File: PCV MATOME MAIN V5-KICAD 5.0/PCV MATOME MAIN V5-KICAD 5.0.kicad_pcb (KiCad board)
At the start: 2 copper layers, 101.6 x 53.3 mm, 14 parts, among them P1 Digital, P10 CONN_01X01, P11 CONN_01X01, P12 CONN_01X01, P13 CONN_01X01, P2 Power, P3 Analog, P4 Analog, P5 PWM, P6 PWM, P7 Communication, P8 CONN_01X01, P9 CONN_01X01, U1 ESP-12F

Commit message: initinal pcb
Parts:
- added C1: 100n, Capacitor_SMD:C_0805_2012Metric_Pad1.15x1.40mm_HandSolder, F.Cu at (113.5, 23.7)
- added C10: 100n, Capacitor_SMD:C_0805_2012Metric_Pad1.15x1.40mm_HandSolder, F.Cu at (52.2, 71.7)
- added C11: 100n, Capacitor_SMD:C_0805_2012Metric_Pad1.15x1.40mm_HandSolder, F.Cu at (111.7, 37.1)
- added C12: 100n, Capacitor_SMD:C_0805_2012Metric_Pad1.15x1.40mm_HandSolder, F.Cu at (102.4, 50.4)
- added C13: 100n, Capacitor_SMD:C_0805_2012Metric_Pad1.15x1.40mm_HandSolder, F.Cu at (106.2, 48.4)
- added C14: 100n, Capacitor_SMD:C_0805_2012Metric_Pad1.15x1.40mm_HandSolder, F.Cu at (102.4, 48.4)
- added C15: 100n, Capacitor_SMD:C_0805_2012Metric_Pad1.15x1.40mm_HandSolder, F.Cu at (106.2, 46.5)
- added C16: 100n, Capacitor_SMD:C_0805_2012Metric_Pad1.15x1.40mm_HandSolder, F.Cu at (80.5, 71.3)
- added C17: 100n, Capacitor_SMD:C_0805_2012Metric_Pad1.15x1.40mm_HandSolder, F.Cu at (84.2, 67.4)
- added C18: 100n, Capacitor_SMD:C_0805_2012Metric_Pad1.15x1.40mm_HandSolder, F.Cu at (115.4, 37.3)
- added C19: 100n, Capacitor_SMD:C_0805_2012Metric_Pad1.15x1.40mm_HandSolder, F.Cu at (111.7, 41.0)
- added C2: 100n, Capacitor_SMD:C_0805_2012Metric_Pad1.15x1.40mm_HandSolder, F.Cu at (113.5, 21.7)
- added C20: 100n, Capacitor_SMD:C_0805_2012Metric_Pad1.15x1.40mm_HandSolder, F.Cu at (59.6, 39.2)
- added C21: 100n, Capacitor_SMD:C_0805_2012Metric_Pad1.15x1.40mm_HandSolder, F.Cu at (91.5, 42.4)
- added C22: 100n, Capacitor_SMD:C_0805_2012Metric_Pad1.15x1.40mm_HandSolder, F.Cu at (91.5, 40.5)
- added C23: 100n, Capacitor_SMD:C_0805_2012Metric_Pad1.15x1.40mm_HandSolder, F.Cu at (91.5, 38.5)
- added C24: 100n, Capacitor_SMD:C_0805_2012Metric_Pad1.15x1.40mm_HandSolder, F.Cu at (113.5, 27.6)
- added C25: 10u, Capacitor_SMD:C_0805_2012Metric_Pad1.15x1.40mm_HandSolder, F.Cu at (113.5, 25.6)
- added C26: 10u, Capacitor_SMD:CP_Elec_4x5.4, F.Cu at (58.1, 43.3)
- added C27: 100u, Capacitor_SMD:CP_Elec_8x6.5, F.Cu at (75.7, 49.5)
- added C28: 100u, Capacitor_SMD:CP_Elec_8x6.5, F.Cu at (95.2, 48.0)
- added C3: 100n, Capacitor_SMD:C_0805_2012Metric_Pad1.15x1.40mm_HandSolder, F.Cu at (113.5, 19.8)
- added C4: 100n, Capacitor_SMD:C_0805_2012Metric_Pad1.15x1.40mm_HandSolder, F.Cu at (59.6, 37.2)
- added C5: 100n, Capacitor_SMD:C_0805_2012Metric_Pad1.15x1.40mm_HandSolder, F.Cu at (39.7, 63.5)
- added C6: 100n, Capacitor_SMD:C_0805_2012Metric_Pad1.15x1.40mm_HandSolder, F.Cu at (37.2, 71.7)
- added C7: 100n, Capacitor_SMD:C_0805_2012Metric_Pad1.15x1.40mm_HandSolder, F.Cu at (41.0, 71.7)
- added C8: 100n, Capacitor_SMD:C_0805_2012Metric_Pad1.15x1.40mm_HandSolder, F.Cu at (44.7, 71.7)
- added C9: 100n, Capacitor_SMD:C_0805_2012Metric_Pad1.15x1.40mm_HandSolder, F.Cu at (48.5, 71.7)
- added D1: D, Diode_SMD:D_SOD-123, F.Cu at (60.1, 35.1)
- added D2: D, Diode_SMD:D_SOD-123, F.Cu at (60.1, 32.7)
- added D3: D, Diode_SMD:D_SOD-123, F.Cu at (60.3, 29.4)
- added D4: D, Diode_SMD:D_SOD-123, F.Cu at (40.2, 61.3)
- added J1: Conn_02x08_Odd_Even, Connector_IDC:IDC-Header_2x08_P2.54mm_Vertical, F.Cu at (262.9, 62.2)
- added J10: Conn_01x02, Connector_JST:JST_EH_B02B-EH-A_1x02_P2.50mm_Vertical, F.Cu at (92.7, 59.6)
- added J11: Conn_01x04, Connector_JST:JST_EH_B04B-EH-A_1x04_P2.50mm_Vertical, F.Cu at (121.4, 59.9)
- added J12: Conn_01x08, Connector_JST:JST_EH_B08B-EH-A_1x08_P2.50mm_Vertical, F.Cu at (86.9, 141.5)
- added J13: Conn_01x08, Connector_JST:JST_EH_B08B-EH-A_1x08_P2.50mm_Vertical, F.Cu at (43.9, 143.0)
- added J14: Conn_01x02, Connector_Wire:SolderWirePad_1x02_P5.08mm_Drill1.5mm, F.Cu at (49.8, 57.7)
- added J15: Conn_01x02, Connector_Wire:SolderWirePad_1x02_P5.08mm_Drill1.5mm, F.Cu at (63.2, 61.0)
- added J2: Conn_02x08_Odd_Even, Connector_IDC:IDC-Header_2x08_P2.54mm_Vertical, F.Cu at (225.3, 62.5)
- added J3: Conn_01x06, Connector_JST:JST_EH_B06B-EH-A_1x06_P2.50mm_Vertical, F.Cu at (236.2, 102.9)
- added J4: Conn_01x06, Connector_JST:JST_EH_B06B-EH-A_1x06_P2.50mm_Vertical, F.Cu at (264.2, 93.7)
- added J6: Conn_01x06, Connector_JST:JST_EH_B06B-EH-A_1x06_P2.50mm_Vertical, F.Cu at (236.2, 94.0)
- added J7: Conn_01x06, Connector_JST:JST_EH_B06B-EH-A_1x06_P2.50mm_Vertical, F.Cu at (264.2, 102.9)
- added J8: Conn_01x08, Connector_JST:JST_EH_B08B-EH-A_1x08_P2.50mm_Vertical, F.Cu at (28.2, 111.0)
- added J9: Conn_01x16, Connector_JST:JST_EH_B16B-EH-A_1x16_P2.50mm_Vertical, F.Cu at (142.2, 132.1)
- added Q1: BSS138, Package_TO_SOT_SMD:SOT-23, F.Cu at (84.1, 70.2)
- added Q2: BSS138, Package_TO_SOT_SMD:SOT-23, F.Cu at (87.8, 67.5)
- added Q3: 2SC1815, Package_TO_SOT_THT:TO-92_Inline, F.Cu at (31.3, 72.3)
- added R1: 10K, Resistor_SMD:R_0805_2012Metric_Pad1.15x1.40mm_HandSolder, F.Cu at (102.4, 46.5)
- added R10: 10K, Resistor_SMD:R_0805_2012Metric_Pad1.15x1.40mm_HandSolder, F.Cu at (88.0, 64.7)
- added R11: 10K, Resistor_SMD:R_0805_2012Metric_Pad1.15x1.40mm_HandSolder, F.Cu at (111.7, 39.1)
- added R12: 10K, Resistor_SMD:R_0805_2012Metric_Pad1.15x1.40mm_HandSolder, F.Cu at (115.4, 35.4)
- added R13: 10K, Resistor_SMD:R_0805_2012Metric_Pad1.15x1.40mm_HandSolder, F.Cu at (100.1, 53.4)
- added R14: 10K, Resistor_SMD:R_0805_2012Metric_Pad1.15x1.40mm_HandSolder, F.Cu at (111.7, 35.2)
- added R15: 10K, Resistor_SMD:R_0805_2012Metric_Pad1.15x1.40mm_HandSolder, F.Cu at (84.2, 65.5)
- added R16: 10K, Resistor_SMD:R_0805_2012Metric_Pad1.15x1.40mm_HandSolder, F.Cu at (80.5, 69.4)
- added R17: 10K, Resistor_SMD:R_0805_2012Metric_Pad1.15x1.40mm_HandSolder, F.Cu at (115.4, 33.4)
- added R18: 100, Resistor_SMD:R_0805_2012Metric_Pad1.15x1.40mm_HandSolder, F.Cu at (80.5, 67.4)
- added R2: 10K, Resistor_SMD:R_0805_2012Metric_Pad1.15x1.40mm_HandSolder, F.Cu at (106.2, 44.5)
- added R3: 20K, Resistor_SMD:R_0805_2012Metric_Pad1.15x1.40mm_HandSolder, F.Cu at (91.4, 62.8)
- added R4: 10K, Resistor_SMD:R_0805_2012Metric_Pad1.15x1.40mm_HandSolder, F.Cu at (102.4, 44.5)
- added R5: 10K, Resistor_SMD:R_0805_2012Metric_Pad1.15x1.40mm_HandSolder, F.Cu at (80.5, 65.5)
- added R6: 10K, Resistor_SMD:R_0805_2012Metric_Pad1.15x1.40mm_HandSolder, F.Cu at (80.5, 63.5)
- added R7: 10K, Resistor_SMD:R_0805_2012Metric_Pad1.15x1.40mm_HandSolder, F.Cu at (113.5, 31.5)
- added R8: 10K, Resistor_SMD:R_0805_2012Metric_Pad1.15x1.40mm_HandSolder, F.Cu at (113.5, 29.5)
- added R9: 10K, Resistor_SMD:R_0805_2012Metric_Pad1.15x1.40mm_HandSolder, F.Cu at (84.2, 63.5)
- added RN1: R_Network08, Resistor_THT:R_Array_SIP9, F.Cu at (31.8, 21.8)
- added RN2: R_Network08, Resistor_THT:R_Array_SIP9, F.Cu at (15.2, 53.3)
- added RV1: R_POT, Potentiometer_THT:Potentiometer_Bourns_3296W_Vertical, F.Cu at (46.2, 34.3)
- added SW1: SW_Push, Button_Switch_THT:SW_DIP_SPSTx01_Slide_9.78x4.72mm_W7.62mm_P2.54mm, F.Cu at (35.6, 43.6)
- added U2: MAX7219, Package_SO:SOIC-24W_7.5x15.4mm_P1.27mm, F.Cu at (273.1, 78.7)
- added U3: MAX7219, Package_SO:SOIC-24W_7.5x15.4mm_P1.27mm, F.Cu at (233.7, 78.7)
- added U4: LM1117-3.3, Package_TO_SOT_SMD:SOT-223-3_TabPin2, F.Cu at (69.3, 77.5)
- added U5: LD1117S50TR_SOT223, Package_TO_SOT_THT:TO-220-3_Vertical, F.Cu at (17.3, 81.8)
- added U6: SHIFT_LEVEL_3.3V_5V, LEEVAWNS:SHIFTLEVEL, F.Cu at (197.6, 131.1)
- moved U1 30.9 mm to (236.2, 137.2)
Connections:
- net +5V renamed HV
- P1 pad 10: (no net) -> RESET_ESP
- P1 pad 11: (no net) -> SW14
- P1 pad 12: (no net) -> SW15
- P1 pad 13: (no net) -> SW12
- P1 pad 14: (no net) -> SW13
- P1 pad 15: (no net) -> SW10
- P1 pad 16: (no net) -> SW11
- P1 pad 17: (no net) -> SW8
- P1 pad 18: (no net) -> SW9
- P1 pad 19: (no net) -> SW6
- P1 pad 20: (no net) -> SW7
- P1 pad 21: (no net) -> SW4
- P1 pad 22: (no net) -> SW5
- P1 pad 23: (no net) -> SW2
- P1 pad 24: (no net) -> SW3
- P1 pad 25: (no net) -> SC4
- P1 pad 26: (no net) -> SW1
- P1 pad 27: (no net) -> SC2
- P1 pad 28: (no net) -> SC3
- P1 pad 29: (no net) -> SCK
- P1 pad 30: (no net) -> SC1
- P1 pad 31: (no net) -> CLK_M
- P1 pad 32: (no net) -> DIN
- P1 pad 33: (no net) -> DIN_M
- P1 pad 34: (no net) -> SC_M
- P1 pad 9: (no net) -> SW16
- P2 pad 4: (no net) -> LV
- P2 pad 8: (no net) -> /Vin
- P3 pad 1: (no net) -> RS
- P3 pad 2: (no net) -> RW
- P3 pad 3: (no net) -> EN
- P3 pad 4: (no net) -> D4
- P3 pad 5: (no net) -> D5
- P3 pad 6: (no net) -> D6
- P3 pad 7: (no net) -> D7
- P5 pad 1: (no net) -> SCL
- P5 pad 2: (no net) -> SDA
- P6 pad 2: (no net) -> SET
- P6 pad 3: (no net) -> HOME
- P6 pad 4: (no net) -> BACK
- P6 pad 5: (no net) -> NEXT
- P6 pad 6: (no net) -> BUZZER
- P7 pad 5: (no net) -> RX5V
- P7 pad 6: (no net) -> TX5V
- U1 pad 1: (no net) -> Net-(R1-Pad2)
- U1 pad 15: (no net) -> GND
- U1 pad 16: (no net) -> Net-(R5-Pad2)
- U1 pad 17: (no net) -> Net-(R7-Pad2)
- U1 pad 18: (no net) -> Net-(R6-Pad2)
- U1 pad 21: (no net) -> RX3.3V
- U1 pad 22: (no net) -> TX3.3V
- U1 pad 3: (no net) -> Net-(R2-Pad1)
- U1 pad 8: (no net) -> LV

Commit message: initilize pcb layout
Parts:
- P1: renamed from P2; moved to B.Cu
- P10, P11, P12, P13, P5, P6, P7, P8, P9: moved to B.Cu
- P2: renamed from P3; moved to B.Cu
- P3: renamed from P4; moved to B.Cu
- P4: renamed from P1; moved to B.Cu
- moved SW1 221.1 mm to (240.6, 126.5), turned to 180 degrees
- moved RN2 200.4 mm to (215.6, 57.1), turned to 180 degrees
- moved C4 183.1 mm to (236.2, 85.3)
- moved J12 177.9 mm to (195.6, 50.0)
- moved C1 164.9 mm to (238.3, 131.6), turned to 180 degrees
- moved R1 161.7 mm to (233.4, 141.3), turned to 90 degrees
- moved R3 160.3 mm to (233.4, 136.9), turned to 90 degrees
- moved RN1 159.4 mm to (187.5, 55.9), turned to 180 degrees
- moved R2 154.4 mm to (233.2, 132.3), turned to 90 degrees
- moved C2 153.9 mm to (231.6, 120.4), turned to 90 degrees
- moved C20 153.7 mm to (211.1, 65.0)
- moved J7 152.0 mm to (167.1, 49.3)
- moved Q3 146.8 mm to (167.9, 126.2), turned to 180 degrees
- moved R4 145.9 mm to (235.7, 103.9)
- moved R6 145.2 mm to (208.5, 132.1)
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- renumbered J11 to J10, J12 to J11, J13 to J12, J14 to J13, J15 to J14, J6 to J5, J7 to J6, J8 to J7, J9 to J8, J10 to J9, U2 to U1, U1 to U2, U6 to U4, U4 to U5, U5 to U6
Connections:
- J3 pad 6: (no net) -> Net-(J3-Pad6)
- J4 pad 6: (no net) -> Net-(J4-Pad6)
- J5 pad 6: (no net) -> Net-(J5-Pad6)
- J6 pad 6: (no net) -> Net-(J6-Pad6)
- J8 pad 10: (no net) -> Net-(J8-Pad10)
- J8 pad 7: (no net) -> Net-(J8-Pad7)
- J8 pad 8: (no net) -> Net-(J8-Pad8)
- J8 pad 9: (no net) -> Net-(J8-Pad9)
- P1 pad 1: (no net) -> Net-(P1-Pad1)
- P1 pad 2: (no net) -> /IOREF
- P1 pad 3: (no net) -> /Reset
- P10 pad 1: (no net) -> Net-(P10-Pad1)
- P11 pad 1: (no net) -> Net-(P11-Pad1)
- P12 pad 1: (no net) -> Net-(P12-Pad1)
- P13 pad 1: (no net) -> Net-(P13-Pad1)
- P2 pad 8: (no net) -> /A7
- P3 pad 1: (no net) -> /A8
- P3 pad 2: (no net) -> /A9
- P3 pad 3: (no net) -> /A10
- P3 pad 4: (no net) -> /A11
- P3 pad 5: (no net) -> /A12
- P3 pad 6: (no net) -> /A13
- P3 pad 7: (no net) -> /A14
- P3 pad 8: (no net) -> /A15
- P4 pad 3: (no net) -> /52(SCK)
- P4 pad 4: (no net) -> /53(SS)
- P4 pad 5: (no net) -> /50(MISO)
- P4 pad 6: (no net) -> /51(MOSI)
- P4 pad 7: (no net) -> /48
- P4 pad 8: (no net) -> /49
- P5 pad 10: (no net) -> /8(**)
- P5 pad 3: (no net) -> /AREF
- P5 pad 5: (no net) -> /13(**)
- P5 pad 6: (no net) -> /12(**)
- P5 pad 7: (no net) -> /11(**)
- P5 pad 8: (no net) -> /10(**)
- P5 pad 9: (no net) -> /9(**)
- P6 pad 1: (no net) -> /7(**)
- P6 pad 7: (no net) -> /1(Tx0)
- P6 pad 8: (no net) -> /0(Rx0)
- P7 pad 1: (no net) -> /14(Tx3)
- P7 pad 2: (no net) -> /15(Rx3)
- P7 pad 3: (no net) -> /16(Tx2)
- P7 pad 4: (no net) -> /17(Rx2)
- P7 pad 7: (no net) -> /20(SDA)
- P7 pad 8: (no net) -> /21(SCL)
- P8 pad 1: (no net) -> Net-(P8-Pad1)
- P9 pad 1: (no net) -> Net-(P9-Pad1)
- U2 pad 10: (no net) -> Net-(U2-Pad10)
- U2 pad 11: (no net) -> Net-(U2-Pad11)
- U2 pad 12: (no net) -> Net-(U2-Pad12)
- U2 pad 13: (no net) -> Net-(U2-Pad13)
- U2 pad 14: (no net) -> Net-(U2-Pad14)
- U2 pad 19: (no net) -> Net-(U2-Pad19)
- U2 pad 2: (no net) -> Net-(U2-Pad2)
- U2 pad 20: (no net) -> Net-(U2-Pad20)
- U2 pad 4: (no net) -> Net-(U2-Pad4)
- U2 pad 5: (no net) -> Net-(U2-Pad5)
- U2 pad 6: (no net) -> Net-(U2-Pad6)
- U2 pad 7: (no net) -> Net-(U2-Pad7)
- U2 pad 9: (no net) -> Net-(U2-Pad9)
- U3 pad 24: (no net) -> Net-(U3-Pad24)
- U4 pad 10: (no net) -> Net-(U4-Pad10)
- U4 pad 3: (no net) -> Net-(U4-Pad3)
- U4 pad 4: (no net) -> Net-(U4-Pad4)
- U4 pad 9: (no net) -> Net-(U4-Pad9)
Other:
- board outline removed

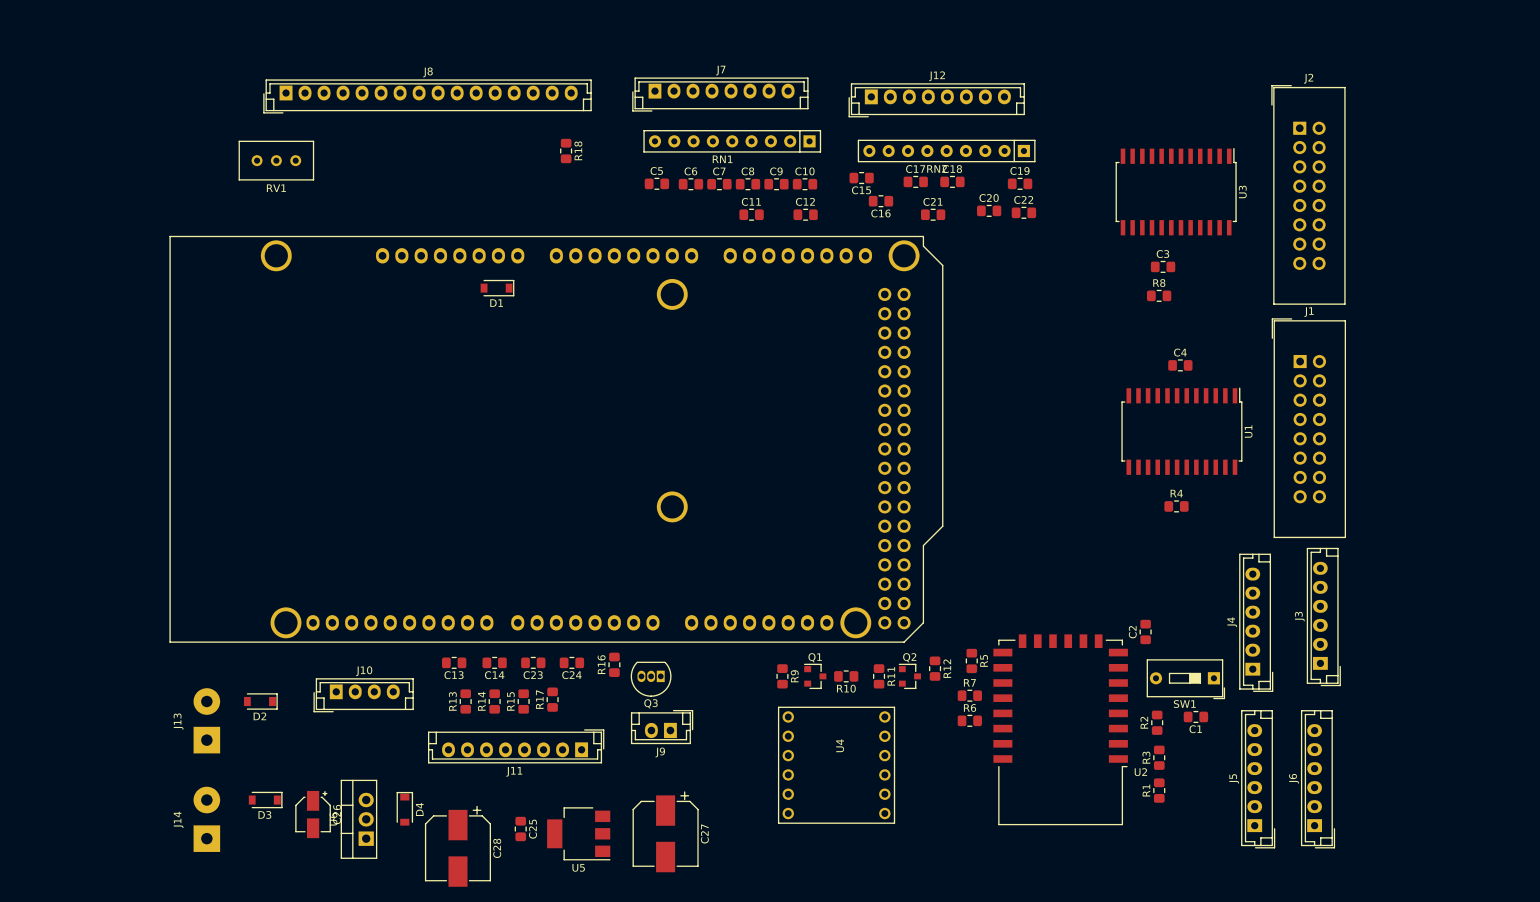
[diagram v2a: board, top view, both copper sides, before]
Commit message: modifier pcb and schematic net list
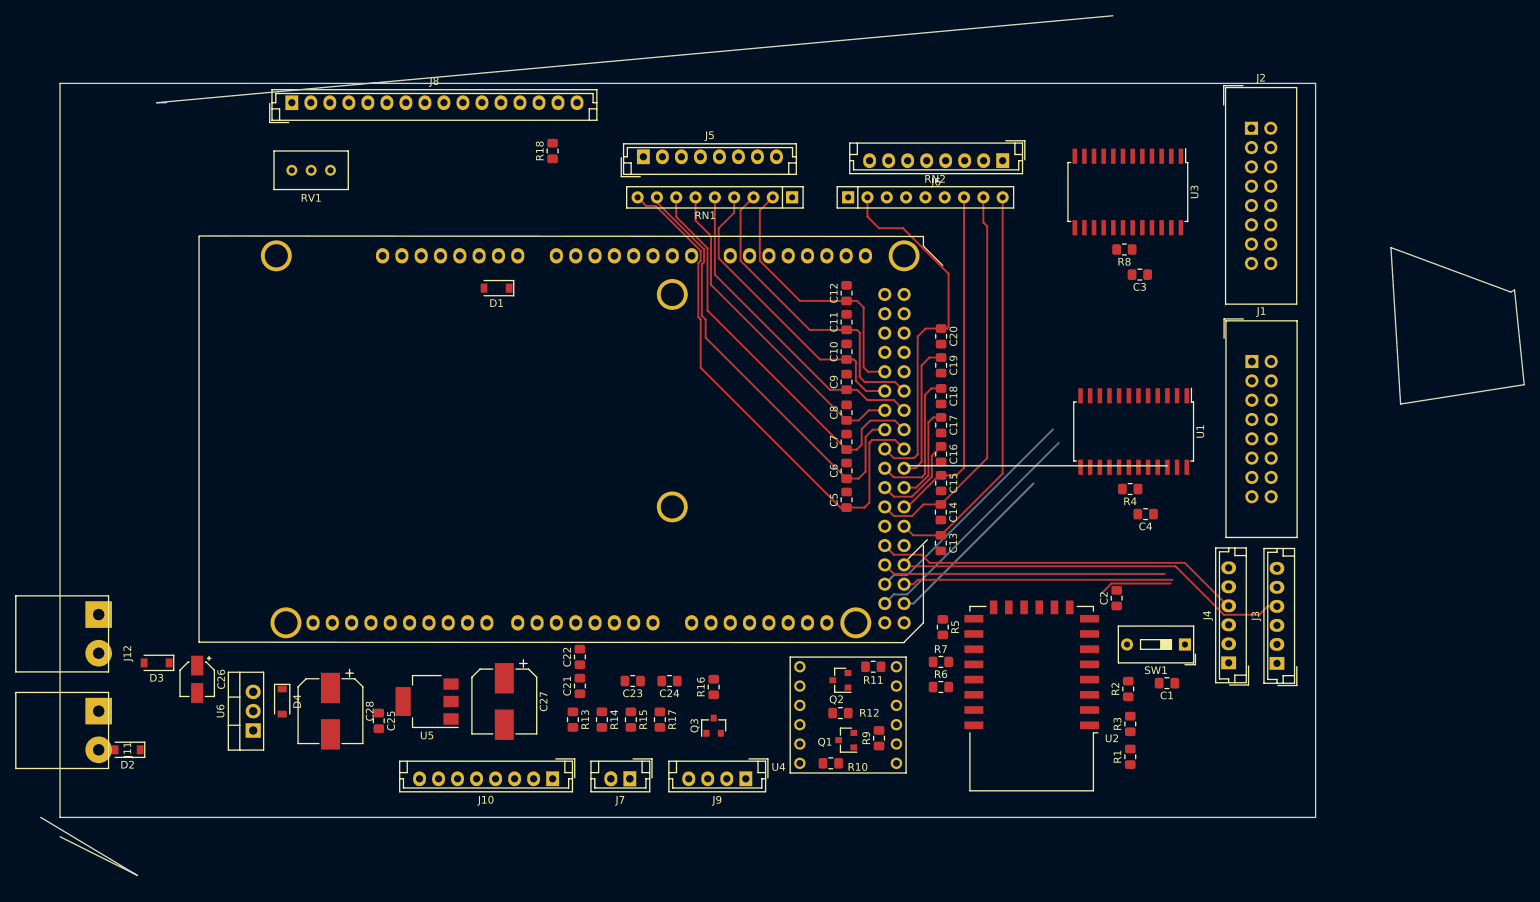
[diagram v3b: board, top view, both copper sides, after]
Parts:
- removed J13, J14: Conn_01x02, Connector_Wire:SolderWirePad_1x02_P5.08mm_Drill1.5mm
- J10: value Conn_01x04 -> Conn_01x08; footprint Connector_JST:JST_EH_B04B-EH-A_1x04_P2.50mm_Vertical -> Connector_JST:JST_EH_B08B-EH-A_1x08_P2.50mm_Vertical
- J11, J12: value Conn_01x08 -> Conn_01x02; footprint Connector_JST:JST_EH_B08B-EH-A_1x08_P2.50mm_Vertical -> LEEVAWNS:SolderWirePad_1x02_P5.08mm_Drill1.5mm
- J5, J6: value Conn_01x06 -> Conn_01x08; footprint Connector_JST:JST_EH_B06B-EH-A_1x06_P2.50mm_Vertical -> Connector_JST:JST_EH_B08B-EH-A_1x08_P2.50mm_Vertical
- J7: value Conn_01x08 -> Conn_01x02; footprint Connector_JST:JST_EH_B08B-EH-A_1x08_P2.50mm_Vertical -> Connector_JST:JST_EH_B02B-EH-A_1x02_P2.50mm_Vertical
- J9: value Conn_01x02 -> Conn_01x04; footprint Connector_JST:JST_EH_B02B-EH-A_1x02_P2.50mm_Vertical -> Connector_JST:JST_EH_B04B-EH-A_1x04_P2.50mm_Vertical
- Q3: footprint Package_TO_SOT_THT:TO-92_Inline -> Package_TO_SOT_SMD:SOT-23
- moved J12 123.7 mm to (94.0, 120.7), turned to 270 degrees
- moved J5 119.2 mm to (165.6, 57.9), turned to 0 degrees
- moved J6 96.6 mm to (212.9, 58.4), turned to 180 degrees
- moved J7 90.5 mm to (163.8, 139.7), turned to 180 degrees
- moved C22 82.6 mm to (157.3, 123.7), turned to 90 degrees
- moved C21 77.4 mm to (157.3, 127.5), turned to 90 degrees
- moved C13 65.9 mm to (204.7, 108.7), turned to 270 degrees
- moved J11 63.6 mm to (94.0, 133.3), turned to 270 degrees
- moved C14 61.9 mm to (204.7, 104.6), turned to 270 degrees
- moved C5 48.5 mm to (192.3, 103.0), turned to 90 degrees
- moved C6 42.9 mm to (192.3, 99.2), turned to 90 degrees
- moved C15 41.5 mm to (204.8, 100.8), turned to 270 degrees
- moved C7 37.8 mm to (192.3, 95.4), turned to 90 degrees
- moved C16 34.2 mm to (204.8, 97.0), turned to 270 degrees
- moved C8 32.7 mm to (192.3, 91.6), turned to 90 degrees
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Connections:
- C13 pad 1: SET -> SW1
- C14 pad 1: HOME -> SW2
- C15 pad 1: SW1 -> SW3
- C16 pad 1: SW2 -> SW4
- C17 pad 1: SW3 -> SW5
- C18 pad 1: SW4 -> SW6
- C19 pad 1: SW5 -> SW7
- C20 pad 1: SW6 -> SW8
- C21 pad 1: SW7 -> SET
- C22 pad 1: SW8 -> HOME
- J10 pad 1: SCL -> NEXT
- J10 pad 2: SDA -> GND
- J10 pad 3: HV -> BACK
- J11 pad 1: NEXT -> GND
- J11 pad 2: GND -> Net-(D2-Pad2)
- J12 pad 1: SW1 -> GND
- J12 pad 2: SW2 -> Net-(D3-Pad2)
- J3 pad 6: Net-(J3-Pad6) -> (no net)
- J4 pad 6: Net-(J4-Pad6) -> (no net)
- J5 pad 1: HV -> SW9
- J5 pad 2: GND -> SW10
- J5 pad 3: DIN -> SW11
- J5 pad 4: SC3 -> SW12
- J5 pad 5: SCK -> SW13
- J5 pad 6: Net-(J5-Pad6) -> SW14
- J6 pad 1: HV -> SW1
- J6 pad 2: GND -> SW2
- J6 pad 3: DIN -> SW3
- J6 pad 4: SC4 -> SW4
- J6 pad 5: SCK -> SW5
- J6 pad 6: Net-(J6-Pad6) -> SW6
- J7 pad 1: SW9 -> HV
- J7 pad 2: SW10 -> Net-(J7-Pad2)
- J8 pad 10: Net-(J8-Pad10) -> (no net)
- J8 pad 7: Net-(J8-Pad7) -> (no net)
- J8 pad 8: Net-(J8-Pad8) -> (no net)
- J8 pad 9: Net-(J8-Pad9) -> (no net)
- J9 pad 1: HV -> SCL
- J9 pad 2: Net-(J9-Pad2) -> SDA
- P1 pad 1: Net-(P1-Pad1) -> (no net)
- P1 pad 2: /IOREF -> (no net)
- P1 pad 3: /Reset -> (no net)
- P10 pad 1: Net-(P10-Pad1) -> (no net)
- P11 pad 1: Net-(P11-Pad1) -> (no net)
- P12 pad 1: Net-(P12-Pad1) -> (no net)
- P13 pad 1: Net-(P13-Pad1) -> (no net)
- P2 pad 8: /A7 -> (no net)
- P3 pad 1: /A8 -> (no net)
- P3 pad 2: /A9 -> (no net)
- P3 pad 3: /A10 -> (no net)
- P3 pad 4: /A11 -> (no net)
- P3 pad 5: /A12 -> (no net)
- P3 pad 6: /A13 -> (no net)
- P3 pad 7: /A14 -> (no net)
- P3 pad 8: /A15 -> (no net)
- P4 pad 25: SC4 -> (no net)
- P4 pad 28: SC3 -> (no net)
- P4 pad 3: /52(SCK) -> (no net)
- P4 pad 4: /53(SS) -> (no net)
- P4 pad 5: /50(MISO) -> (no net)
- P4 pad 6: /51(MOSI) -> (no net)
- P4 pad 7: /48 -> (no net)
- P4 pad 8: /49 -> (no net)
- P5 pad 10: /8(**) -> (no net)
- P5 pad 3: /AREF -> (no net)
- P5 pad 5: /13(**) -> (no net)
- P5 pad 6: /12(**) -> (no net)
- P5 pad 7: /11(**) -> (no net)
- P5 pad 8: /10(**) -> (no net)
- P5 pad 9: /9(**) -> (no net)
- P6 pad 1: /7(**) -> (no net)
- P6 pad 7: /1(Tx0) -> (no net)
- P6 pad 8: /0(Rx0) -> (no net)
- P7 pad 1: /14(Tx3) -> (no net)
- P7 pad 2: /15(Rx3) -> (no net)
- P7 pad 3: /16(Tx2) -> (no net)
- P7 pad 4: /17(Rx2) -> (no net)
- P7 pad 7: /20(SDA) -> SDA
- P7 pad 8: /21(SCL) -> SCL
- P8 pad 1: Net-(P8-Pad1) -> (no net)
- P9 pad 1: Net-(P9-Pad1) -> (no net)
- Q3 pad 2: Net-(J9-Pad2) -> Net-(J7-Pad2)
- U2 pad 10: Net-(U2-Pad10) -> (no net)
- U2 pad 11: Net-(U2-Pad11) -> (no net)
- U2 pad 12: Net-(U2-Pad12) -> (no net)
- U2 pad 13: Net-(U2-Pad13) -> (no net)
- U2 pad 14: Net-(U2-Pad14) -> (no net)
- U2 pad 19: Net-(U2-Pad19) -> (no net)
- U2 pad 2: Net-(U2-Pad2) -> (no net)
- U2 pad 20: Net-(U2-Pad20) -> (no net)
- U2 pad 4: Net-(U2-Pad4) -> (no net)
- U2 pad 5: Net-(U2-Pad5) -> (no net)
- U2 pad 6: Net-(U2-Pad6) -> (no net)
- U2 pad 7: Net-(U2-Pad7) -> (no net)
- U2 pad 9: Net-(U2-Pad9) -> (no net)
- U3 pad 24: Net-(U3-Pad24) -> (no net)
- U4 pad 10: Net-(U4-Pad10) -> (no net)
- U4 pad 3: Net-(U4-Pad3) -> (no net)
- U4 pad 4: Net-(U4-Pad4) -> (no net)
- U4 pad 9: Net-(U4-Pad9) -> (no net)
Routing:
- net SW9: track 0.00 -> 70.0 mm
- net SW10: track 0.00 -> 57.9 mm
- net SW11: track 0.00 -> 53.3 mm
- net SW1: track 0.00 -> 53.1 mm
- net SC1: track 0.00 -> 52.2 mm
- net SW2: track 0.00 -> 51.6 mm
- net SW8: track 0.00 -> 48.9 mm
- net SC2: track 0.00 -> 48.5 mm
- net SW3: track 0.00 -> 45.6 mm
- net SW12: track 0.00 -> 43.1 mm
- net SW13: track 0.00 -> 42.4 mm
- net SW15: track 0.00 -> 41.1 mm
- net CLK_M: track 0.00 -> 40.1 mm
- net SW14: track 0.00 -> 39.4 mm
- net SCK: track 0.00 -> 37.3 mm
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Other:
- board outline added: 195.1 x 113 mm
